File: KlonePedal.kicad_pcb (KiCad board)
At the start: 2 copper layers, 57.5 x 92.1 mm, 68 parts, among them J1 Jack-DC, J2 NMJ4HCD2, J4 NMJ4HCD2, SW1 SW_DPDT_x2, U1 TL072, U2 TL072, U3 MAX1044CPA+

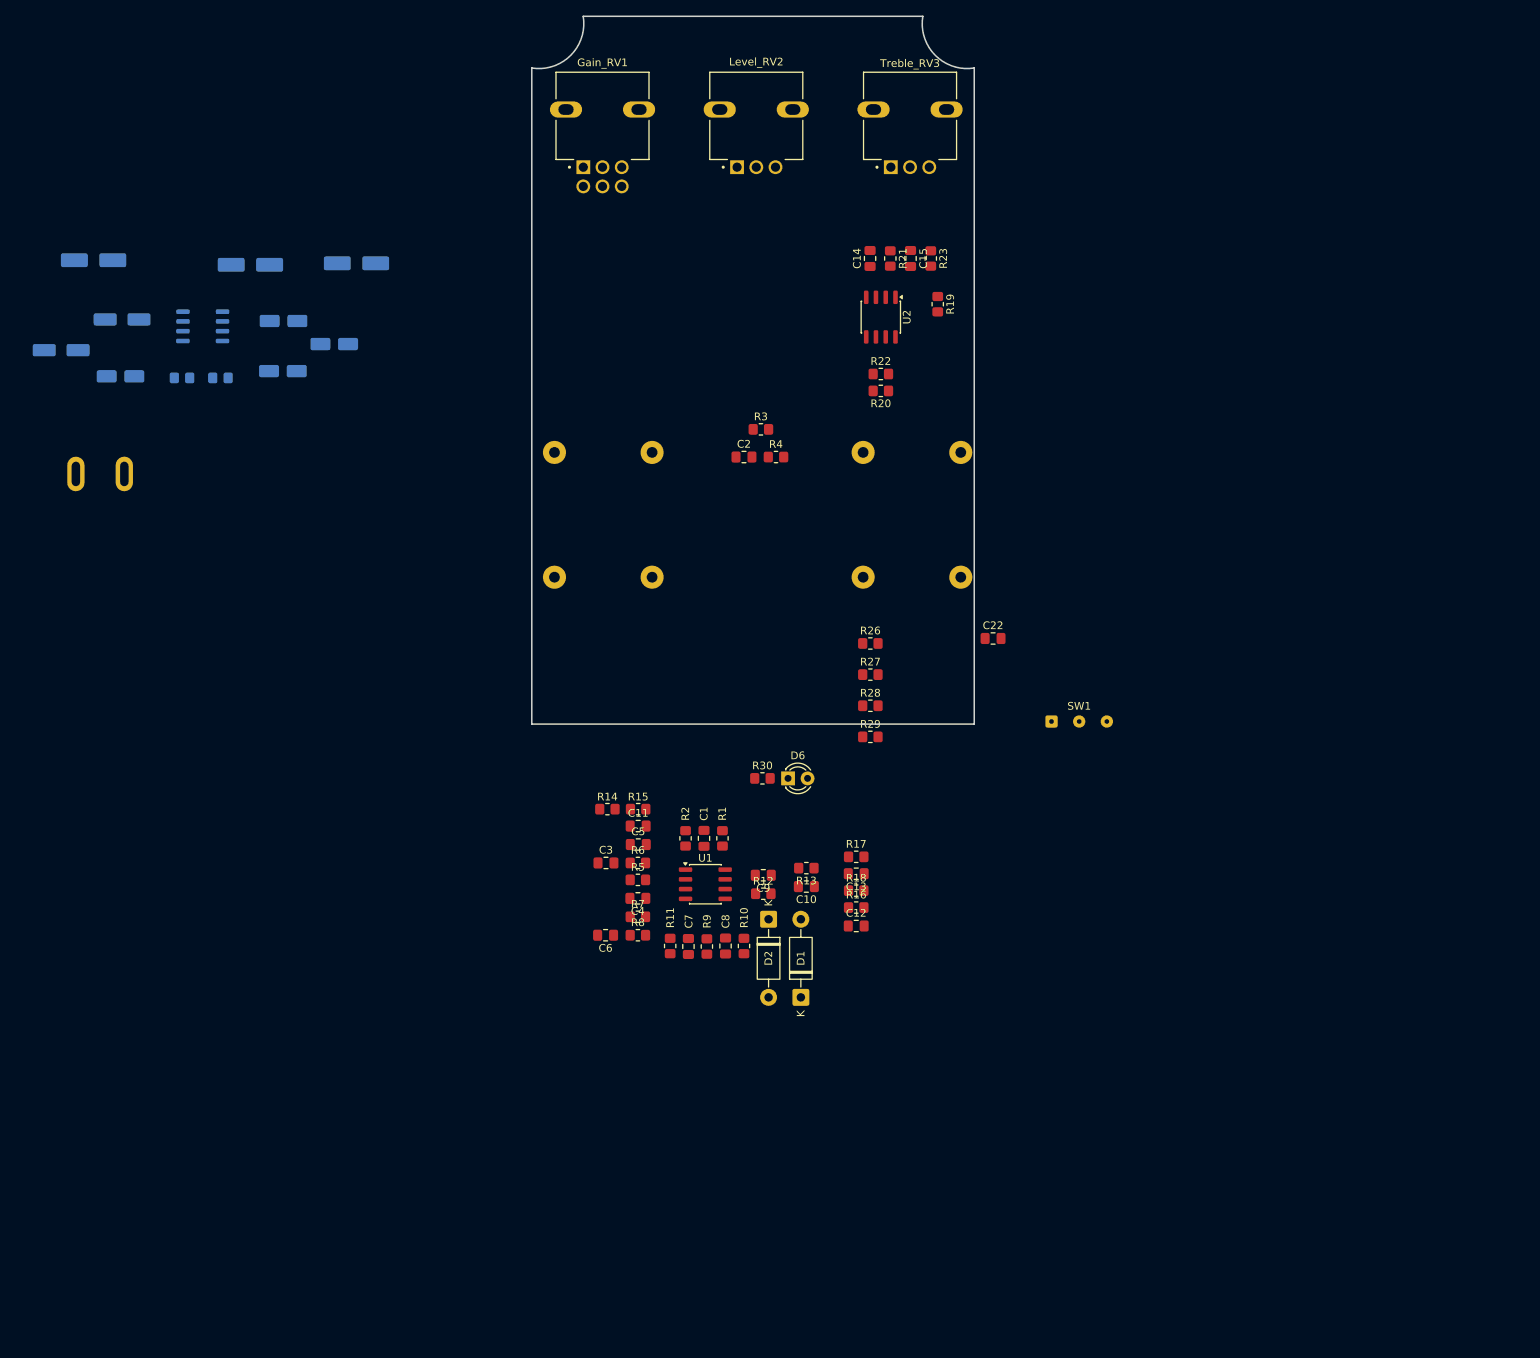
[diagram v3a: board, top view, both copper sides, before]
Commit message: First routing of power circuit
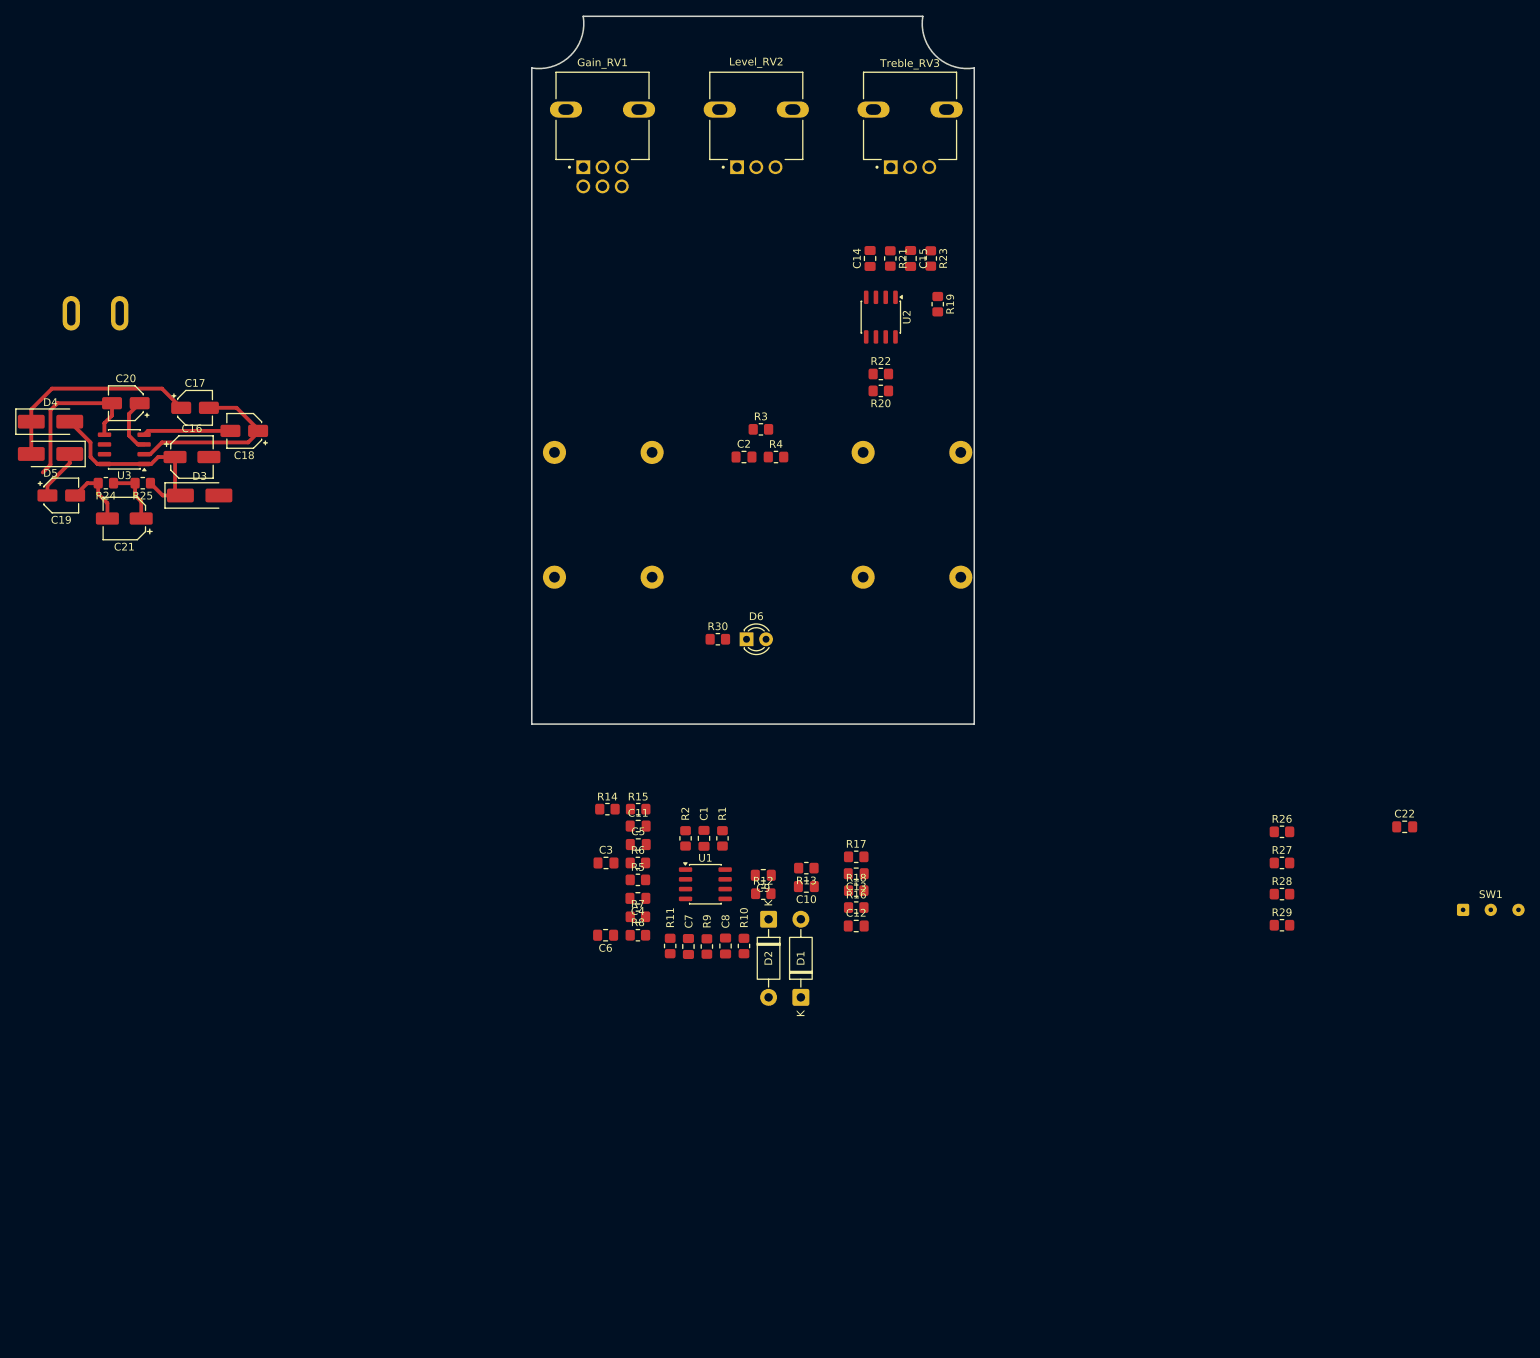
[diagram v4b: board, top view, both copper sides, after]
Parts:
- C16, C17, C18, C19, C20, C21, D3, D4, D5, R24, R25, U3: moved to F.Cu
- moved C22 58.9 mm to (232.3, 138.3)
- moved R27 58.9 mm to (216.4, 143.0)
- moved R28 58.9 mm to (216.4, 147.1)
- moved R29 58.9 mm to (216.4, 151.1)
- moved SW1 58.9 mm to (239.9, 149.1)
- moved R26 58.9 mm to (216.4, 138.9)
- moved D5 46.9 mm to (56.2, 89.8)
- moved C19 40.6 mm to (57.6, 95.2)
- moved D3 33.6 mm to (75.6, 95.2), turned to 0 degrees
- moved D4 33.0 mm to (56.2, 85.6), turned to 0 degrees
- moved C21 23.4 mm to (65.8, 98.2)
- moved J1 20.9 mm to (65.2, 71.5)
- moved C16 20.1 mm to (74.6, 90.2), turned to 0 degrees
- moved R30 19.0 mm to (143.0, 113.9)
- moved U3 19.0 mm to (65.8, 89.2)
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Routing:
- net Net-(D4-K): track 0.00 -> 27.5 mm
- net +9V: track 0.00 -> 27.3 mm
- net Net-(U3-CAP+): track 0.00 -> 24.0 mm
- net -8V6: track 0.00 -> 21.4 mm
- net GND: track 0.00 -> 16.0 mm
- net Net-(U3-CAP-): track 0.00 -> 11.4 mm
- net +4V5: track 0.00 -> 7.73 mm
- net +16V2: track 0.00 -> 6.60 mm

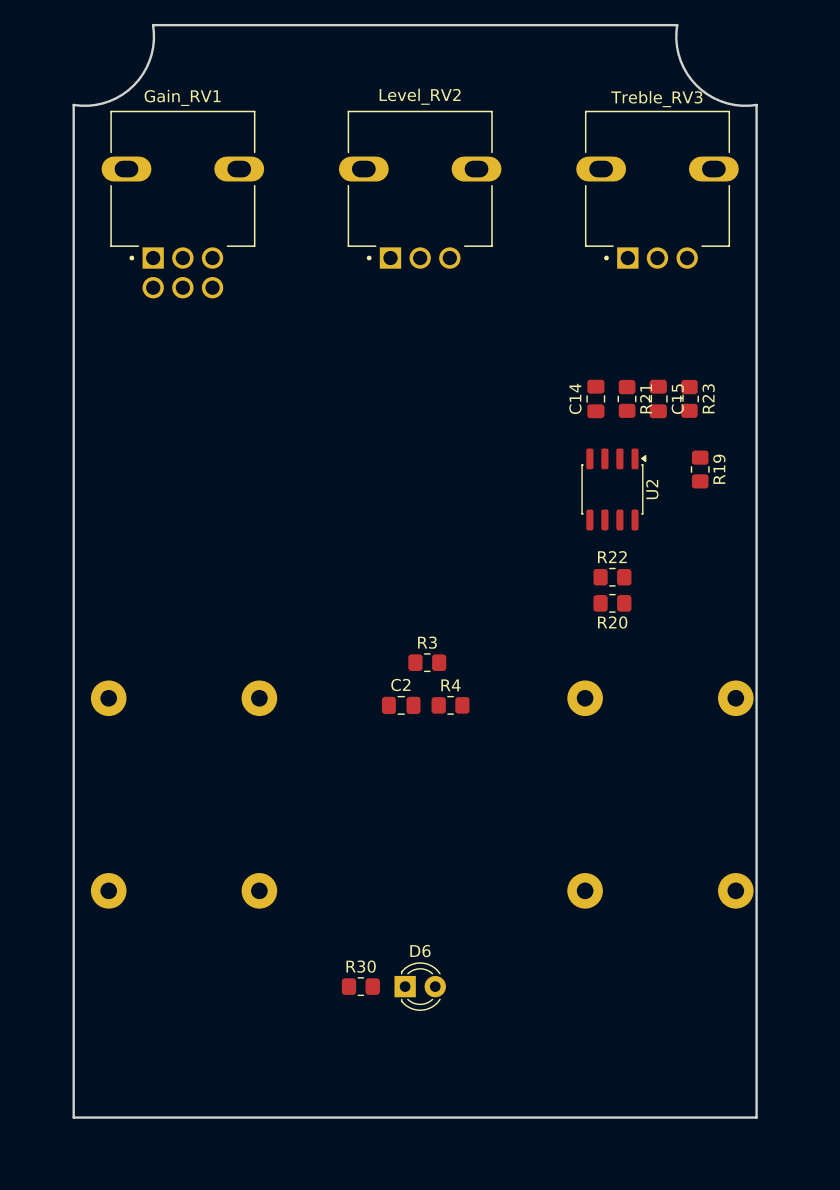
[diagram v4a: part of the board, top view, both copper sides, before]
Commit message: Updated PCB Outline
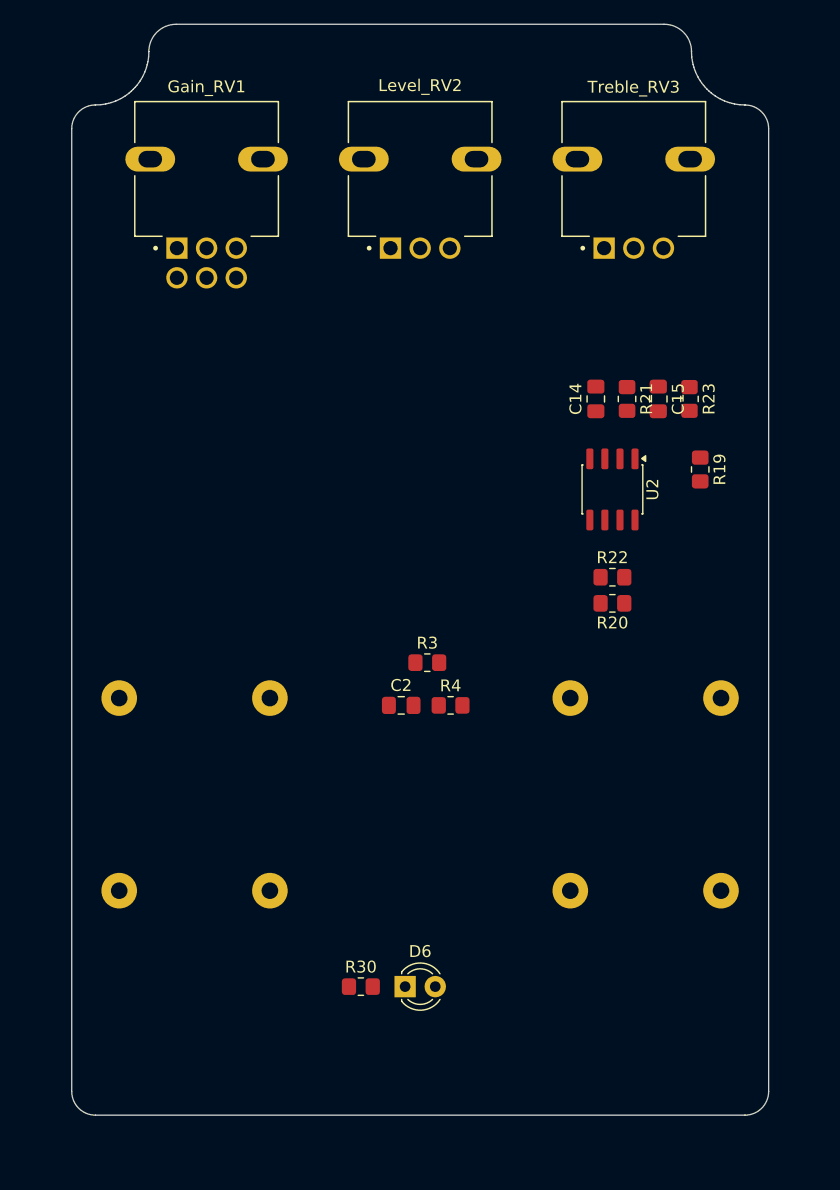
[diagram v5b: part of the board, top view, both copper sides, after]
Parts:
- moved Gain_RV1 2.17 mm to (130.0, 44.2)
- moved Treble_RV3 2.17 mm to (166.0, 44.2)
- moved J4 1.25 mm to (167.0, 97.7)
- moved J2 0.89 mm to (129.1, 97.7)
- moved Level_RV2 0.83 mm to (148.0, 44.2)
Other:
- board size 57.5 x 92.1 mm -> 58.7 x 91.9 mm

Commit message: initial layout
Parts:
- removed SW1: SW_DPDT_x2, Connector_Wire:SolderWire-0.1sqmm_1x03_P3.6mm_D0.4mm_OD1mm
- added J3: SW1B_DPDT_x2, Connector_JST:JST_XH_S3B-XH-A_1x03_P2.50mm_Horizontal, B.Cu at (128.6, 121.4)
- added J5: SW1A_DPDT_x2, Connector_JST:JST_XH_S3B-XH-A_1x03_P2.50mm_Horizontal, B.Cu at (172.4, 121.4)
- J2: value NMJ4HCD2 -> NMJ4HCD2_input
- J4: value NMJ4HCD2 -> NMJ4HCD2_output
- moved C22 114.6 mm to (157.0, 52.0)
- moved D4 109.7 mm to (161.2, 117.3), turned to 180 degrees
- moved D5 107.6 mm to (161.2, 113.1), turned to 0 degrees
- moved R26 107.2 mm to (157.0, 49.7)
- moved C19 103.0 mm to (159.8, 107.7), turned to 180 degrees
- moved C20 92.9 mm to (151.4, 119.7), turned to 0 degrees
- moved R24 92.0 mm to (154.0, 109.3), turned to 0 degrees
- moved U3 89.3 mm to (151.6, 113.7), turned to 0 degrees
- moved C21 86.1 mm to (151.6, 104.7), turned to 0 degrees
- moved C3 84.0 mm to (128.5, 59.0)
- moved C9 83.9 mm to (144.4, 60.8)
- moved R12 83.9 mm to (144.4, 63.2)
- moved R5 83.9 mm to (128.5, 61.4)
- moved C4 83.9 mm to (128.5, 63.8)
- moved R7 83.8 mm to (128.5, 66.3)
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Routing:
- net +4V5: track 7.73 -> 124.6 mm, vias 0 -> 4
- net -8V6: track 21.4 -> 106.2 mm, vias 0 -> 2
- net Net-(J5-Pin_1): track 0.00 -> 82.5 mm
- net Net-(D1-A): track 0.00 -> 77.8 mm, vias 0 -> 1
- net GainOutput: track 0.00 -> 65.0 mm, vias 0 -> 7
- net +9V: track 27.3 -> 88.9 mm
- net Input: track 0.00 -> 48.4 mm, vias 0 -> 4
- net +16V2: track 6.60 -> 53.8 mm, vias 0 -> 2
- net BypassSignal: track 0.00 -> 43.8 mm, vias 0 -> 2
- net Net-(U1B-+): track 0.00 -> 41.3 mm, vias 0 -> 1
- net Net-(J5-Pin_2): track 0.00 -> 40.8 mm
- net OutputSignal: track 0.00 -> 36.6 mm, vias 0 -> 2
- net Net-(D6-K): track 0.00 -> 33.1 mm, vias 0 -> 1
- net Net-(Gain_RV1-Pad5): track 0.00 -> 31.5 mm, vias 0 -> 1
- net Net-(Gain_RV1-Pad1): track 0.00 -> 29.7 mm
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
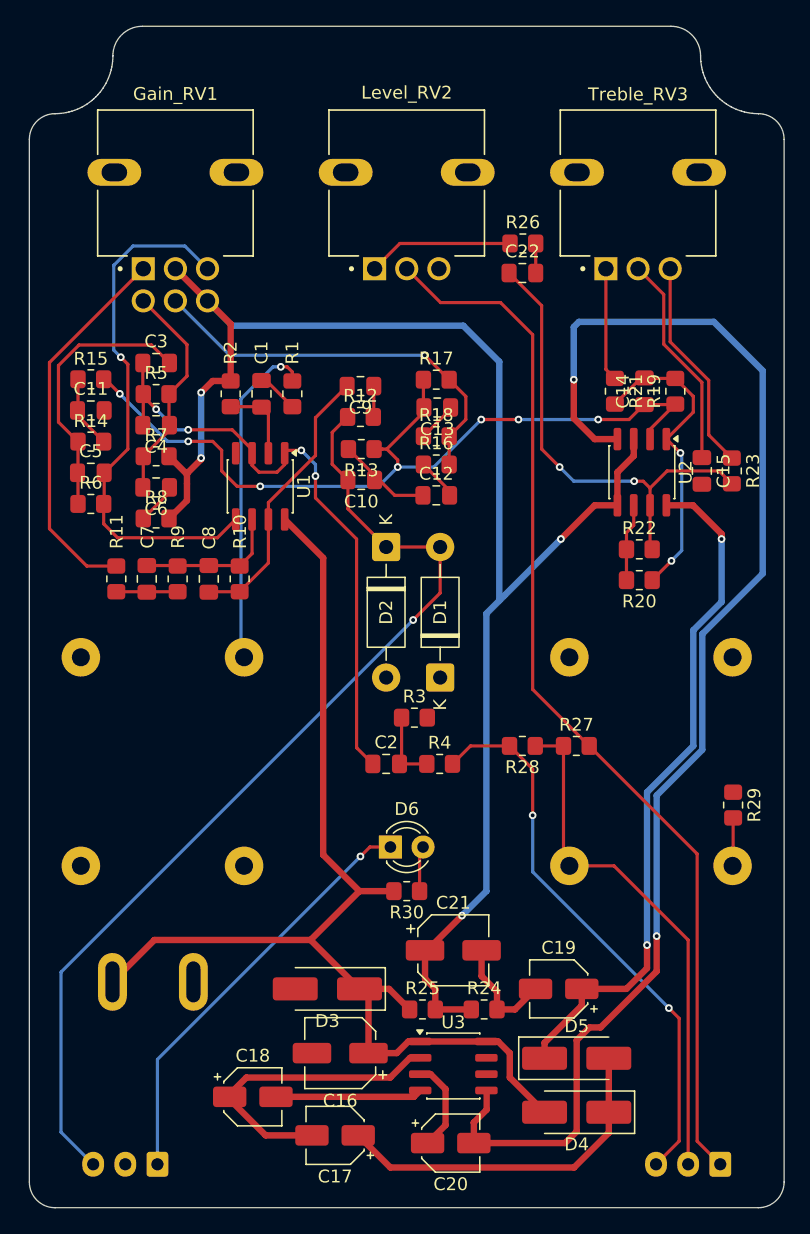
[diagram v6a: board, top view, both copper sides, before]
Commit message: Added ground pours
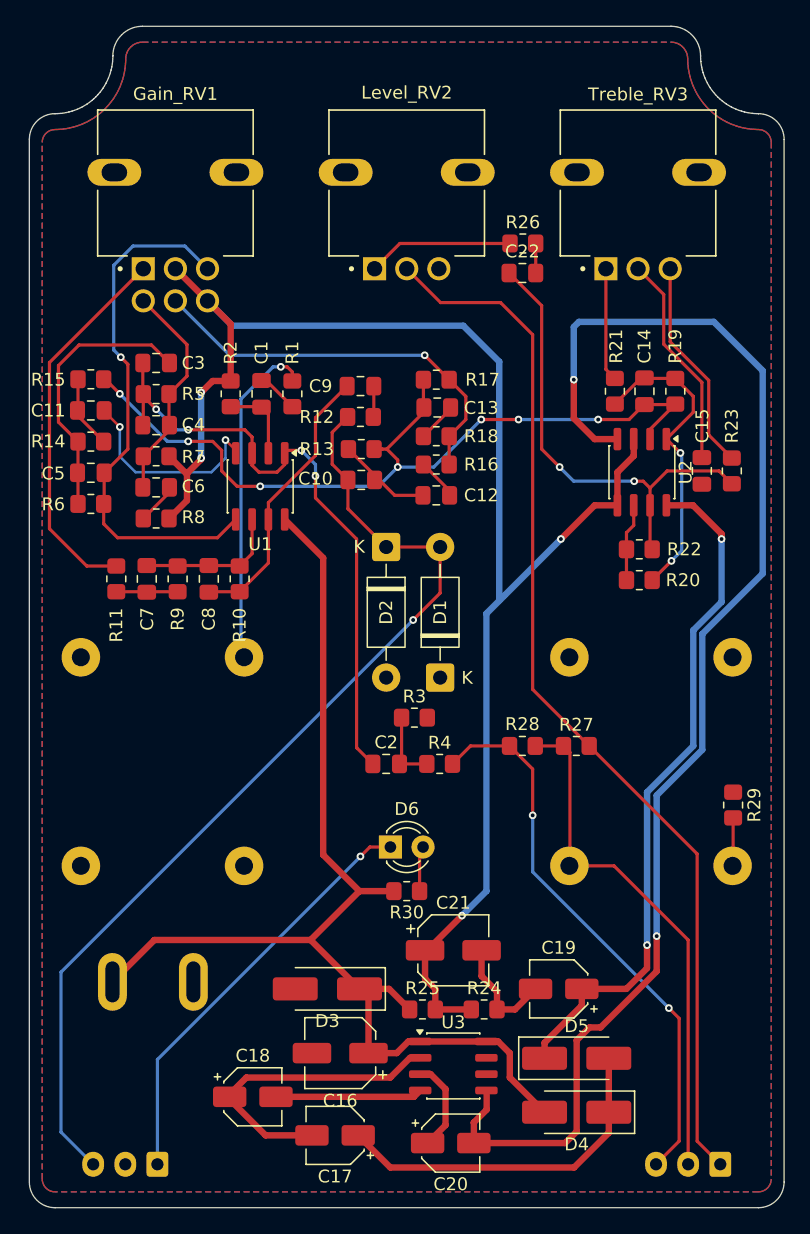
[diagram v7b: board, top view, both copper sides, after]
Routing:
- net GND: track 16.0 -> 32.0 mm, vias 0 -> 2
- net Input: track 48.4 -> 49.0 mm
- added copper zone on B.Cu, net GND
- added copper zone on F.Cu, net GND
